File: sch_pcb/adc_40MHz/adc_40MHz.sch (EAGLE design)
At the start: 22 parts, among them IC2 AD9235BC, X1 BU-SMA-H, X2 BU-SMA-H

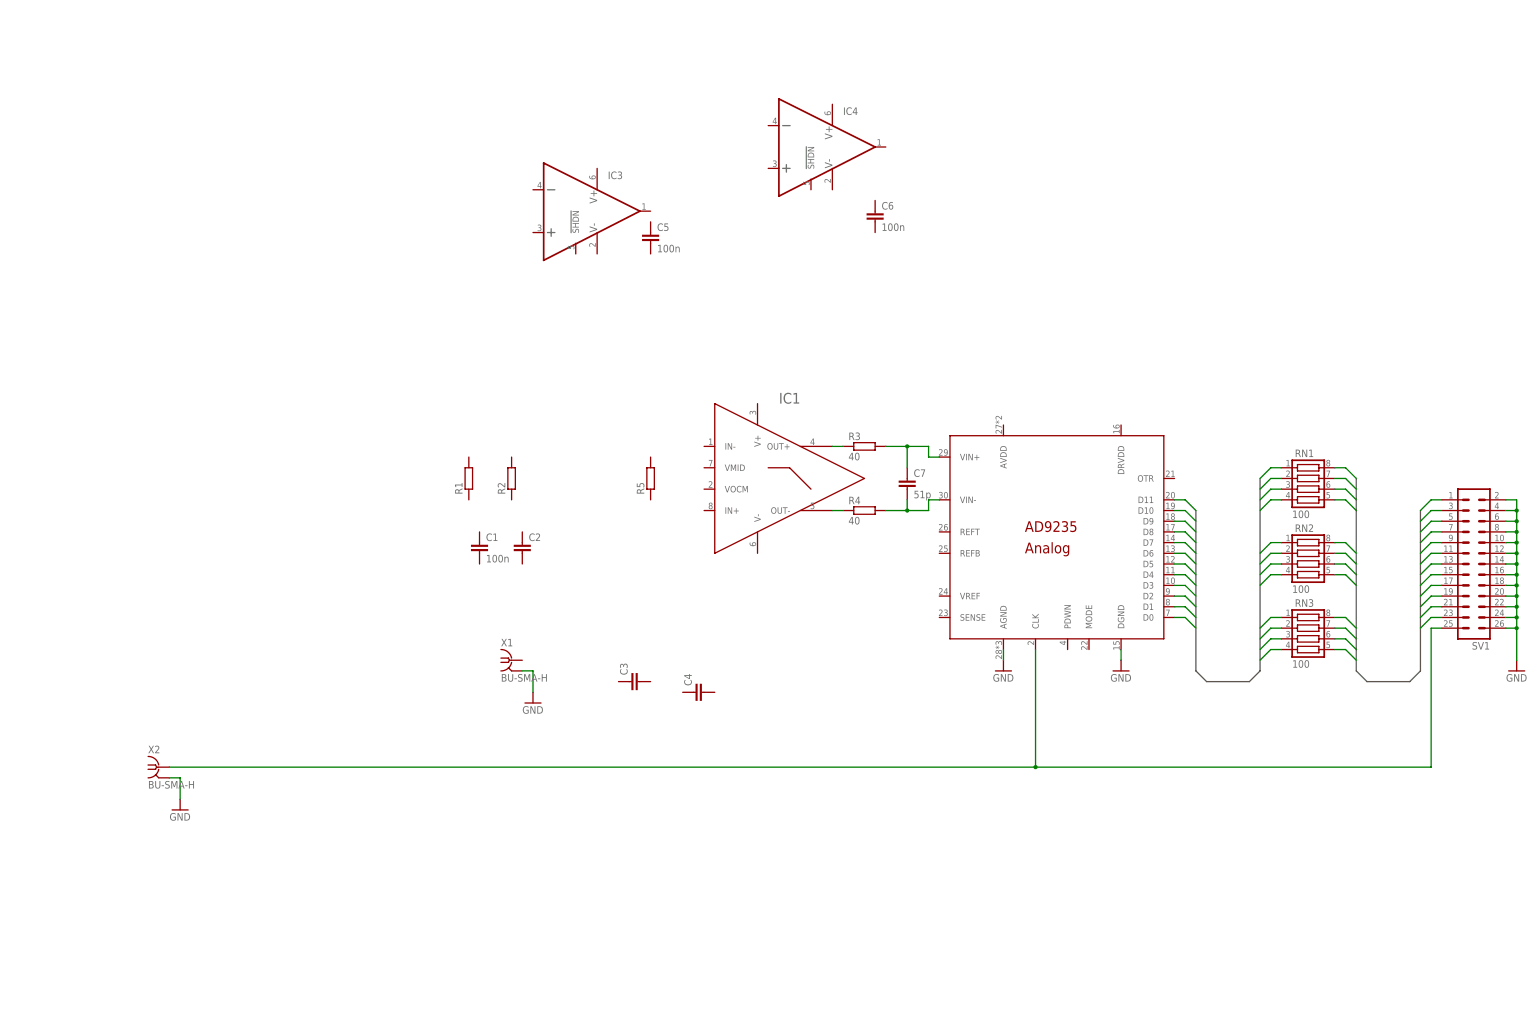
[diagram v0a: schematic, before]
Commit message: Dodano: footptinty do wzmacniacza ltc6252 i innych z pdf. Dodano schemat blokowy i footprint przetwornika ltc2227. Dodano symulacje dla 2 filtrów lt6600 polaczonych kaskadowo
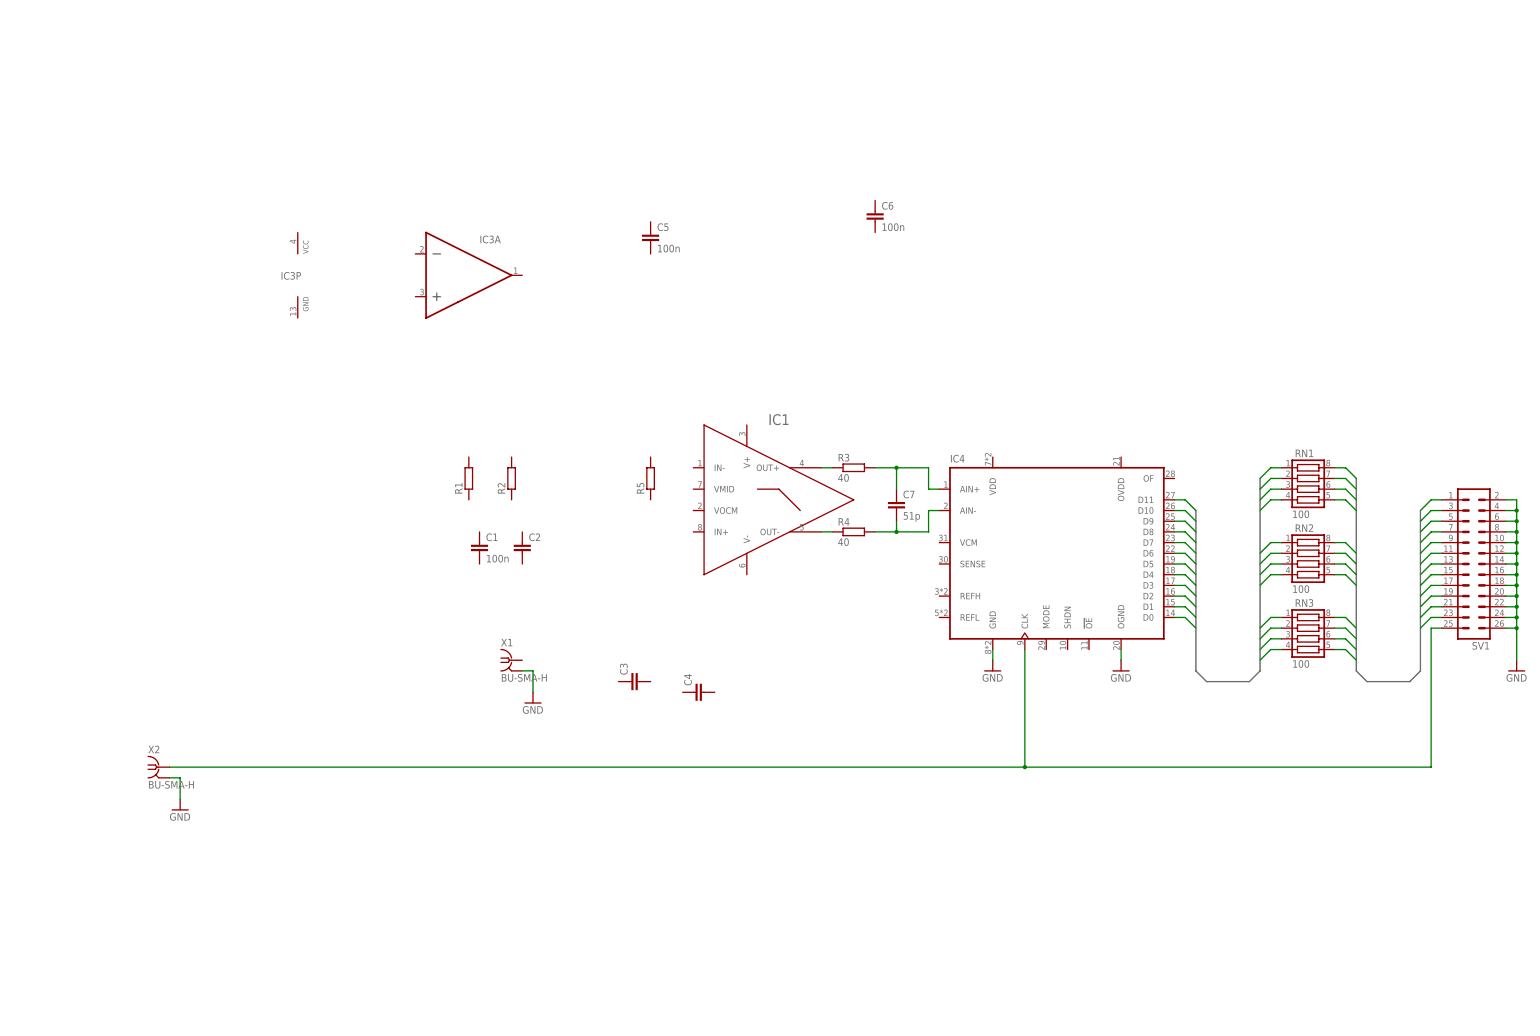
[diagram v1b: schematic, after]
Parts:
- removed IC2: AD9235BC, ad9235:AD9235BC
- IC3: device ltc625x:LTC6252 -> ltc625x:LTC6254XMS
- IC4: device ltc625x:LTC6252 -> ltc22xx:LTC2227
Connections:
- net ADC_D0: now also IC4.D0; no longer IC2.D0
- net ADC_D1: now also IC4.D1; no longer IC2.D1
- net ADC_D10: now also IC4.D10; no longer IC2.D10
- net ADC_D11: now also IC4.D11; no longer IC2.D11
- net ADC_D2: now also IC4.D2; no longer IC2.D2
- net ADC_D3: now also IC4.D3; no longer IC2.D3
- net ADC_D4: now also IC4.D4; no longer IC2.D4
- net ADC_D5: now also IC4.D5; no longer IC2.D5
- net ADC_D6: now also IC4.D6; no longer IC2.D6
- net ADC_D7: now also IC4.D7; no longer IC2.D7
- net ADC_D8: now also IC4.D8; no longer IC2.D8
- net ADC_D9: now also IC4.D9; no longer IC2.D9
- net GND: now also IC4.OGND; no longer IC2.AGND, IC2.DGND
- net N$2: no longer IC2.VIN+
- net N$3: no longer IC2.VIN-
- net N$7: no longer IC2.CLK
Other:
- moved on the sheet: C7, IC1, R3, R4

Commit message: Schemat dokonczony. Do sprawdzenia. Pozostaje plytka
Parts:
- removed IC4: (no value), ltc22xx:LTC2227
- added C10, C11, C16: 100n, rcl:C-EUC0805
- added C12, C14, C15, C23: 100n, rcl:C-EUC0603
- added C13, C18, C9: 1u, rcl:C-EUC0805
- added C17, C21, C22, C8: 2.2u, rcl:C-EUC0805
- added C19: 5p, rcl:C-EUC0603
- added C20: 40p, rcl:C-EUC0603
- added IC2: LT6600-15, lt6600:LT6600-15
- added IC5: LT1521XST, lt1521:LT1521XST
- added JP1: (no value), pinhead:PINHD-1X3/90
- added JP2: (no value), pinhead:PINHD-1X1
- added R10: 10R, rcl:R-EU_R0603
- added R11: 20k, rcl:R-EU_R0603
- added R12: 10k, rcl:R-EU_R0603
- added R13, R14: 100k, rcl:R-EU_R0603
- added R15, R25, R26: DNP, rcl:R-EU_R0603
- added R16: 270R 0.1%, rcl:R-EU_R0603
- added R17: 300R 0.1%, rcl:R-EU_R0603
- added R18: 4.7R 0.1%, rcl:R-EU_R0603
- added R19, R24, R7, R8: 0R, rcl:R-EU_R0603
- added R20: 910R, rcl:R-EU_R0603
- added R21, R6: 100R, rcl:R-EU_R0603
- added R22, R23: 560R 0.1%, rcl:R-EU_R0603
- added R9: 50R 0.1%, rcl:R-EU_R0603
- added RN4: LT5400-1, lt5400:LT5400
- C1: value 100n -> 20p
- C2: value (none) -> 5p
- C3: value (none) -> 1u
- C4: value (none) -> 100n; device rcl:C-EUC0805 -> rcl:C-EUC0603
- C6: value 100n -> 2.2u; device rcl:C-EUC0603 -> rcl:C-EUC0805
- C7: value 51p -> 51pF
- IC1: value (none) -> LTC2227; device lt6600:LT6600-15 -> ltc22xx:LTC2227
- IC3: value (none) -> LTC6254XMS
- R1: value (none) -> 430
- R2: value (none) -> 10R
- R5: value (none) -> 2.4k
- RN1, RN2, RN3: value 100 -> 100R
- X1: value BU-SMA-H -> SIGNAL
- X2: value BU-SMA-H -> CLK
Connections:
- new net +3V3: C11.1, C12.1, C14.1, C15.1, C16.1, C17.1, C3.1, C5.1, C8.1, C9.1, IC1.OVDD, IC1.VDD, IC2.V+, IC3P.V+, IC5.OUT, R11.2, R13.2, R24.2, RN4.1
- new net CLK: IC1.CLK, SV1.25, X2.1
- new net N$10: IC1.SHDN, R7.2
- new net N$11: R16.1, R9.2, X1.1
- new net N$12: IC3D.+IN, R13.1, R14.2
- new net N$13: IC3C.OUT, R21.1, R22.1
- new net N$14: IC3D.-IN, R10.1
- new net N$15: IC3D.OUT, R10.2, R15.2
- new net N$16: RN4.7, RN4.8
- new net N$17: IC3C.-IN, R21.2
- new net N$18: IC2.VMID, IC3C.+IN
- new net N$19: R16.2, R18.1
- new net N$20: C20.1, R17.1, R18.2, R20.1
- new net N$21: R17.2, R19.1
- new net N$22: C19.2, IC3A.OUT, R19.2, R5.1
- new net N$23: C19.1, IC3A.-IN, R20.2
- new net N$24: IC3A.+IN, RN4.5, RN4.6
- new net N$25: RN4.2, RN4.3
- new net N$26: IC3B.-IN, R2.1
- new net N$27: C1.1, IC3B.OUT, R2.2, R23.2
- new net N$28: C1.2, R1.1, R5.2
- new net N$29: C2.1, IC3B.+IN, R1.2
- new net N$30: IC2.IN+, R22.2
- new net N$31: IC2.IN-, R23.1
- new net N$32: IC1.MODE, R11.1, R12.2
- new net N$33: C13.2, C4.1, C6.1, IC1.REFH
- new net N$35: C23.1, IC1.SENSE, R24.1, R25.1, R26.2
- new net N$5: C22.1, IC1.VCM, IC2.VOCM, R25.2
- new net N$6: IC1.OF, R6.1
- new net N$8: JP2.1, R6.2
- new net N$9: IC1.!OE, R8.2
- new net VIN: C10.1, C21.1, IC5.IN, JP1.1
- net ADC_D0: now also IC1.D0; no longer IC4.D0
- net ADC_D1: now also IC1.D1; no longer IC4.D1
- net ADC_D10: now also IC1.D10; no longer IC4.D10
- net ADC_D11: now also IC1.D11; no longer IC4.D11
- net ADC_D2: now also IC1.D2; no longer IC4.D2
- net ADC_D3: now also IC1.D3; no longer IC4.D3
- net ADC_D4: now also IC1.D4; no longer IC4.D4
- net ADC_D5: now also IC1.D5; no longer IC4.D5
- net ADC_D6: now also IC1.D6; no longer IC4.D6
- net ADC_D7: now also IC1.D7; no longer IC4.D7
- net ADC_D8: now also IC1.D8; no longer IC4.D8
- net ADC_D9: now also IC1.D9; no longer IC4.D9
- net GND: now also C10.2, C11.2, C12.2, C13.1, C14.2, C15.2, C16.2, C17.2, C18.1, C2.2, C20.2, C21.2, C22.2, C23.2, C3.2, C5.2, C8.2, C9.2, IC1.GND, IC1.OGND, IC2.V-, IC3P.V-, IC5.GND, JP1.2, R12.1, R14.1, R15.1, R26.1, R7.1, R8.1, R9.1, RN4.4, RN4.EP; no longer IC4.OGND
- net N$1: now also IC2.OUT+; no longer IC1.OUT+
- net N$2: now also IC1.AIN+
- net N$3: now also IC1.AIN-
- net N$4: now also IC2.OUT-; no longer IC1.OUT-
- net N$7: now also C18.2, C4.2, C6.2, IC1.REFL; no longer SV1.25, X2.1
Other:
- moved on the sheet: C1, C2, C3, C4, C5, C6, C7, IC3A, IC3P, R1, R2, R3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

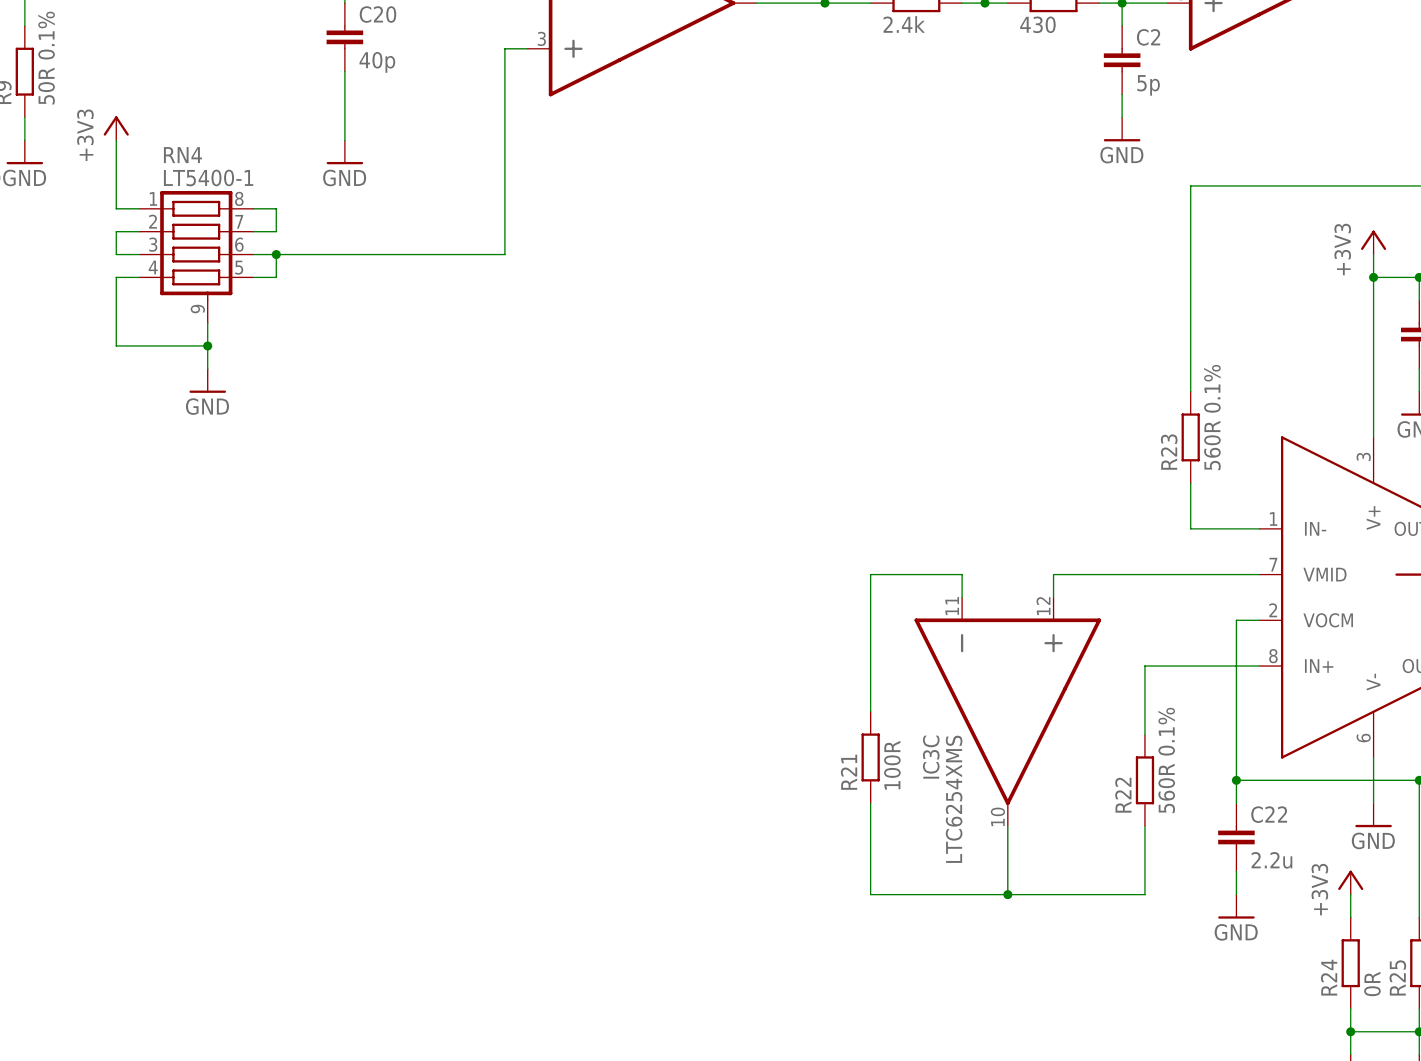
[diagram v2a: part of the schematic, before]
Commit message: Drobna zmiana - dodano kondensator Vmid
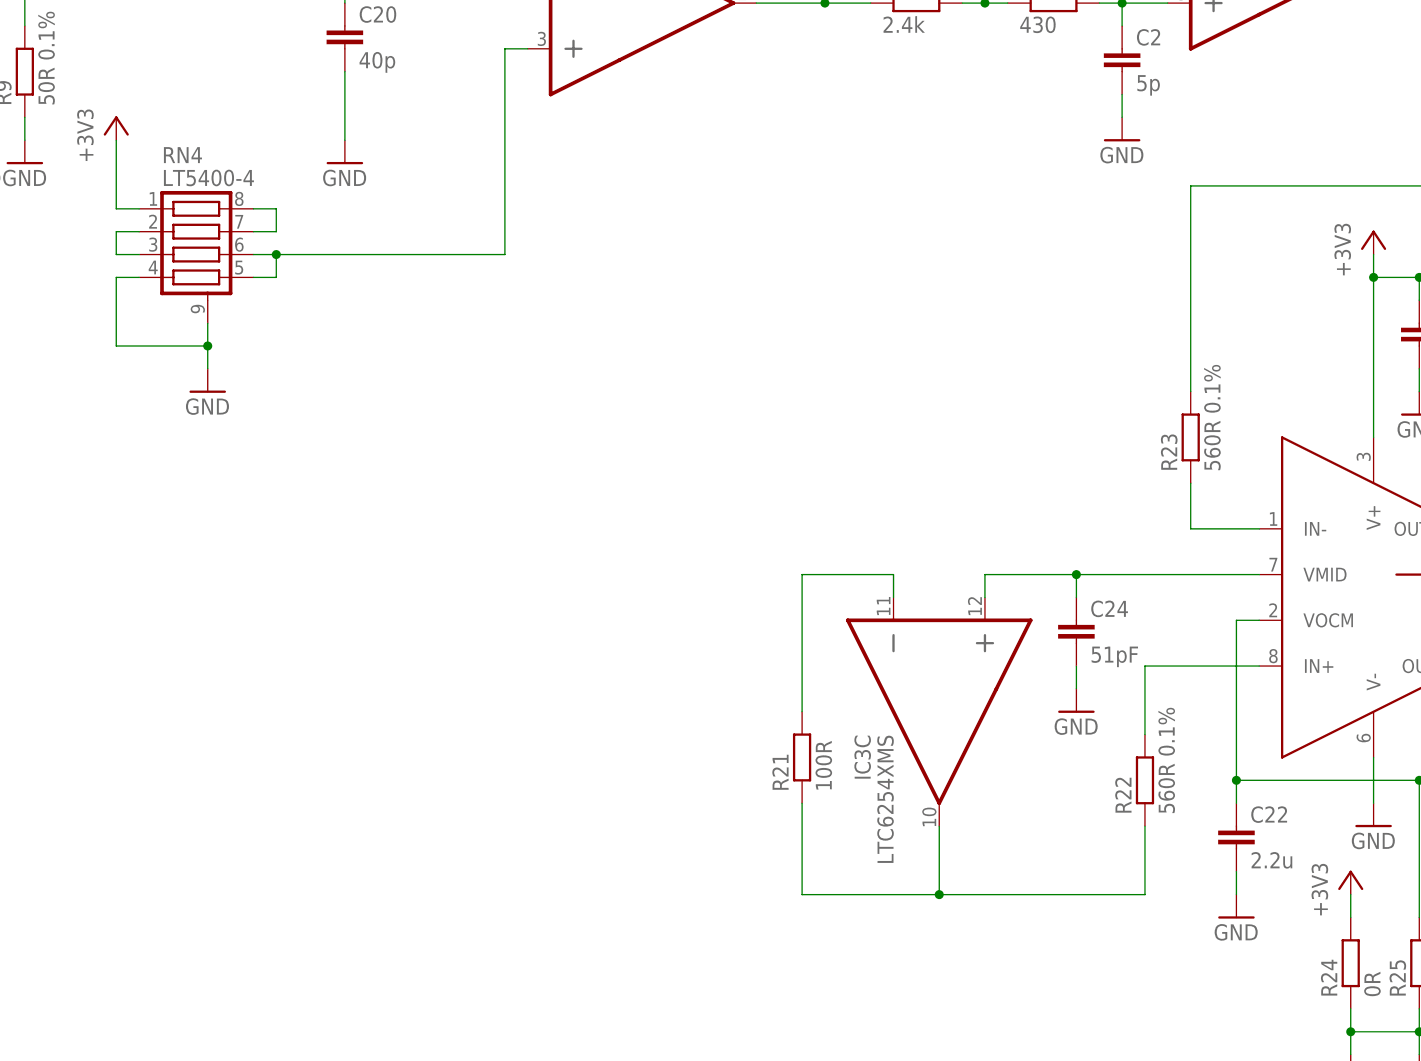
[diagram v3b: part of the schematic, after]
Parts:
- added C24: 51pF, rcl:C-EUC0603
- RN4: value LT5400-1 -> LT5400-4
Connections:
- net GND: now also C24.2
- net N$18: now also C24.1
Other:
- moved on the sheet: IC3C, R21
